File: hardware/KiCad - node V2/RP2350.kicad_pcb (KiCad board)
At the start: 4 copper layers, 55.6 x 52 mm, 83 parts, among them J1 Input, J2 Output, J3 USB_C_Receptacle_USB2.0_14P, J4 Screw_Terminal_01x08, SW1 BOOTSEL, U1 RP2350A, U2 THVD1450D, U3 ADXL355BEZ, U4 TPS2121RUXR, U5 USBLC6-2SC6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

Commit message: KiCad: J1 terminal update
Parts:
- added J5: IN/OUT Terminal, footprints:CONN-TH_B8B-XH-A-LF-SN, F.Cu at (176.5, 79.9)
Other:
- board size 55.6 x 52 mm -> 145.6 x 52.6 mm

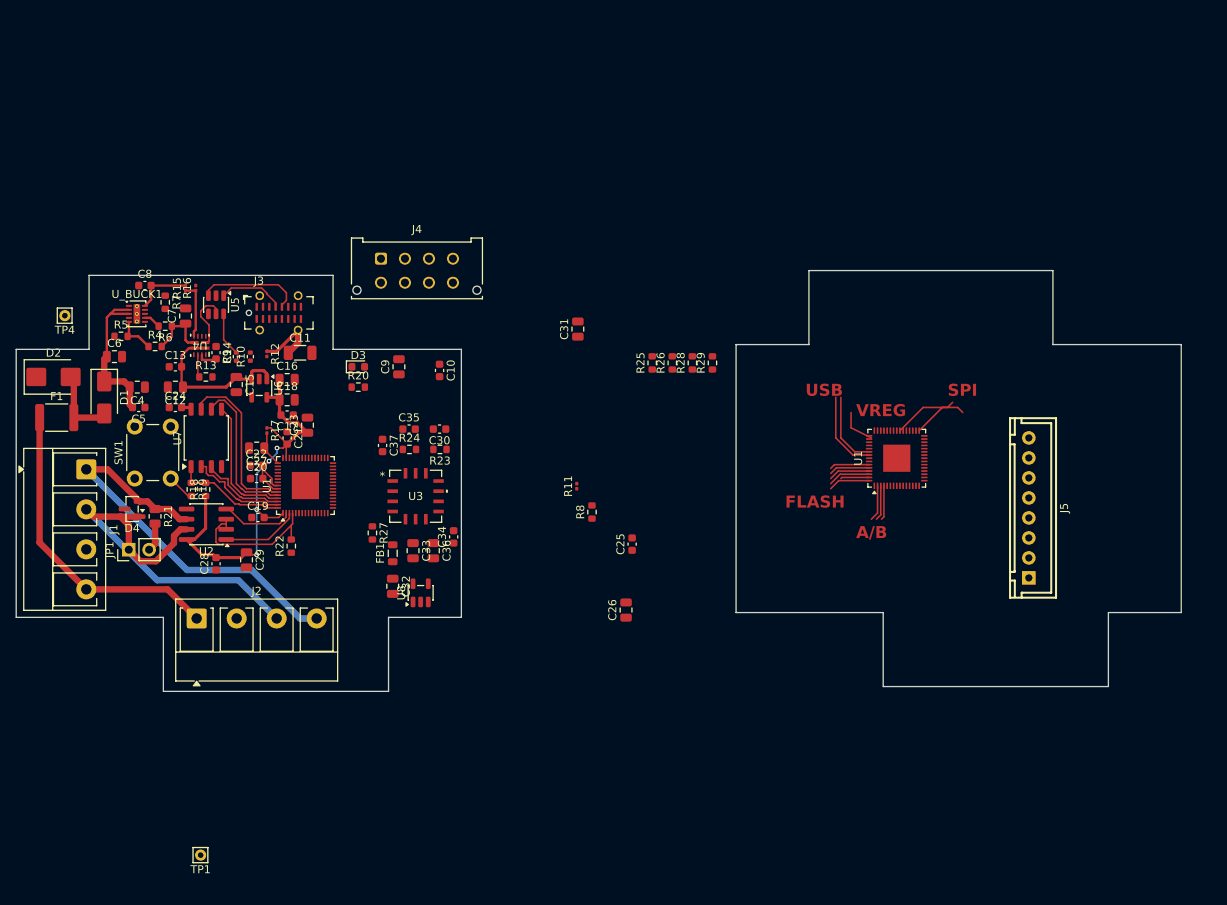
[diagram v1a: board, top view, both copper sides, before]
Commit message: hardware: added net classes
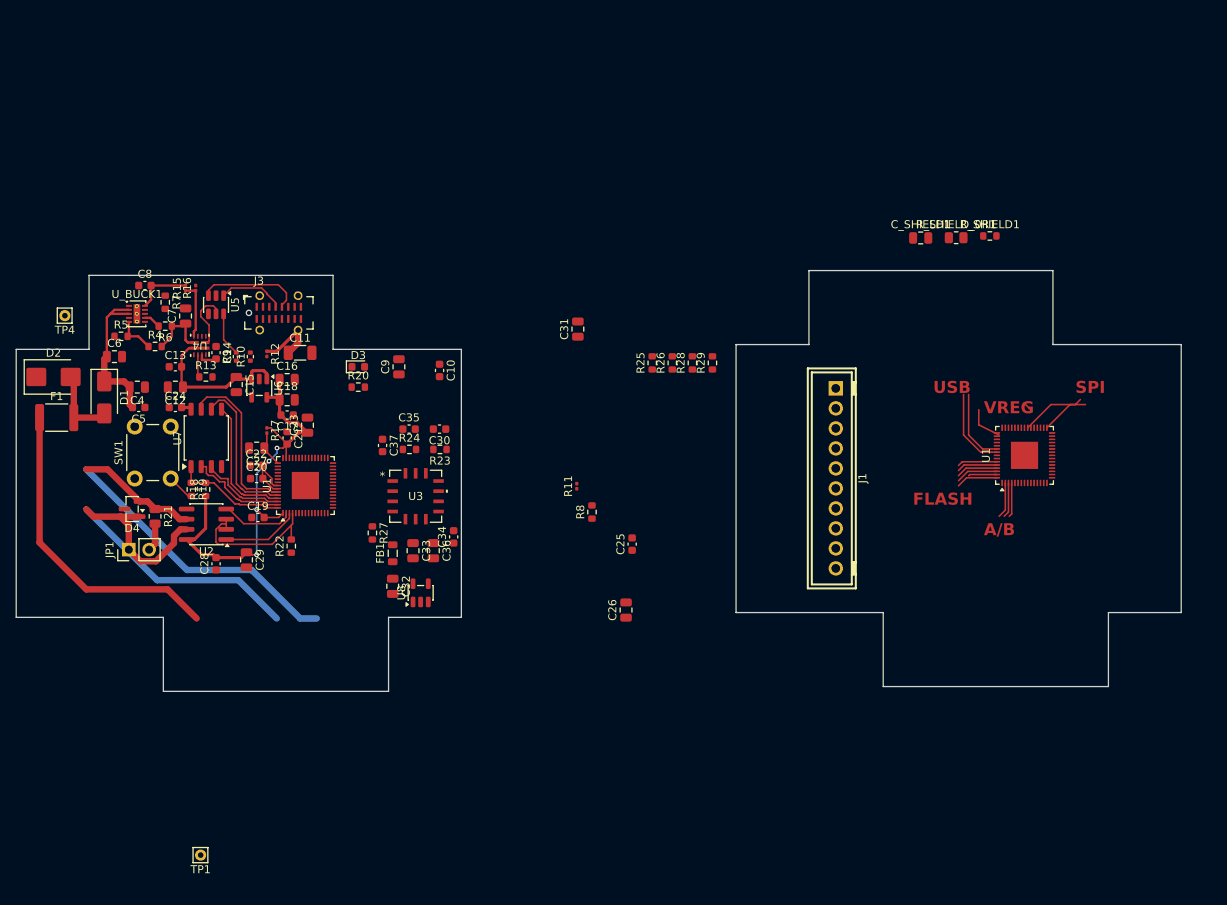
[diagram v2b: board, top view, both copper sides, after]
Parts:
- removed J2: Output, my_footprints:TerminalBlock_RND_205-00278_1x04_P5.00mm_Vertical
- removed J4: Screw_Terminal_01x08, Connector_Molex:Molex_Micro-Fit_3.0_43045-0812_2x04_P3.00mm_Vertical
- removed J5: IN/OUT Terminal, footprints:CONN-TH_B8B-XH-A-LF-SN
- added C_SHIELD1: 10nF, Capacitor_SMD:C_0805_2012Metric, F.Cu at (163.0, 46.1)
- added R_SHIELD1: 1M, Resistor_SMD:R_0603_1608Metric, F.Cu at (171.7, 45.9)
- added R_SHIELD_0R1: 0R DNP, Resistor_SMD:R_0805_2012Metric, F.Cu at (167.4, 46.1)
- J1: value Input -> JST-XH-10; footprint TerminalBlock_RND:TerminalBlock_RND_205-00278_1x04_P5.00mm_Vertical -> footprints:CONN-TH_10P-P2.50_B10B-XH-A-LF-SN
- moved J1 93.7 mm to (152.4, 76.2)
- moved U1 16.0 mm to (176.0, 73.3)
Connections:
- F1 pad 1: Net-(J1-12V) -> Net-(J1-12VIN)
- J1 pad 1: Net-(J1-12V) -> Net-(J1-12VIN)
- J1 pad 2: GND -> Net-(J1-12VIN)
- J1 pad 3: Net-(D4-A2) -> GND
- J1 pad 4: Net-(D4-A1) -> GND
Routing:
- net Net-(J1-12VIN): track 0.00 -> 39.2 mm
- net Net-(J1-12V): track 39.2 -> 0.00 mm

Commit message: hardware: 2 terminals fix
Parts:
- removed J1: JST-XH-10, footprints:CONN-TH_10P-P2.50_B10B-XH-A-LF-SN
- added J_IN1: JST-GH-5, footprints:CONN-SMD_BM05B-GHS-TBT, F.Cu at (189.2, 64.4)
- added J_OUT1: JST-GH-5, footprints:CONN-SMD_BM05B-GHS-TBT, F.Cu at (189.2, 70.7)
- moved F1 128.9 mm to (177.8, 29.4), turned to 90 degrees
- moved D4 125.2 mm to (189.6, 75.9), turned to -90 degrees
- moved D2 123.1 mm to (172.7, 28.6), turned to 90 degrees
- moved R_SHIELD_0R1 42.5 mm to (193.0, 80.0), turned to 180 degrees
- moved C_SHIELD1 41.6 mm to (193.0, 74.9), turned to 180 degrees
- moved R_SHIELD1 38.2 mm to (193.0, 77.5), turned to 180 degrees
- moved U1 15.9 mm to (167.7, 86.8), turned to 0 degrees
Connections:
- net Net-(D4-A1) renamed /RS485_B
- net Net-(D4-A2) renamed /RS485 A
- net Net-(J1-SH_IN) renamed /SHIELD
- F1 pad 1: Net-(J1-12VIN) -> /12V_BUS
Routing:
- net Net-(J1-12VIN): track 39.2 -> 0.00 mm
- net /RS485 A: track 51.6 -> 13.6 mm
- net (no net): track 15.0 -> 51.5 mm
- net /SHIELD: track 0.00 -> 14.2 mm
- net Net-(D1-A): track 9.27 -> 0.00 mm
- net GND: track 0.00 -> 6.35 mm, vias 0 -> 1
- net /12V_BUS: track 0.00 -> 6.35 mm
- net /RS485_B: track 51.1 -> 48.4 mm
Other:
- board size 145.6 x 52.6 mm -> 145.6 x 52 mm
- board text removed: "SPI"

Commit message: hardware: layout progress + many footprints
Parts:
- removed the U1 at (86.1, 77.1)
- added R2: 5.1k, Resistor_SMD:R_0402_1005Metric, F.Cu at (167.6, 68.7)
- added R3: 5.1k, Resistor_SMD:R_0402_1005Metric, F.Cu at (159.7, 62.4)
- C24: footprint Capacitor_SMD:C_0603_1608Metric -> Capacitor_SMD:C_0402_1005Metric
- J3: footprint my_footprints:USB_C_Receptacle_G-Switch_GT-USB-7051x -> footprints:USB-C-SMD_GT-USB-7051A
- R11: footprint Resistor_SMD:R_0201_0603Metric -> Resistor_SMD:R_0805_2012Metric
- R12: footprint Resistor_SMD:R_0201_0603Metric -> Resistor_SMD:R_0603_1608Metric
- SW1: footprint Button_Switch_THT:SW_PUSH_6mm -> footprints:KEY-SMD_4P-L4.2-W3.2-P2.20-LS4.6
- U5: footprint Package_TO_SOT_SMD:SOT-23-6 -> footprints:USBLC6-2SC6
- U7: footprint Package_SO:SOIC-8_5.3x5.3mm_P1.27mm -> footprints:WSON-8_L6.0-W5.0-P1.27-BL-EP
- moved D1 123.2 mm to (184.2, 64.8), turned to 90 degrees
- moved U6 111.2 mm to (190.8, 51.9)
- moved U2 103.5 mm to (177.2, 83.8), turned to 90 degrees
- moved U4 100.5 mm to (172.8, 70.6), turned to -90 degrees
- moved R12 94.4 mm to (175.7, 62.2), turned to 0 degrees
- moved SW1 92.0 mm to (155.9, 63.3), turned to 0 degrees
- moved U5 91.1 mm to (164.8, 69.7)
- moved U_BUCK1 90.9 mm to (155.9, 54.3)
- moved C11 87.3 mm to (172.7, 63.8), turned to -90 degrees
- moved R9 87.3 mm to (163.8, 73.7)
- moved R10 86.8 mm to (165.1, 73.7)
- moved J3 83.0 mm to (165.3, 64.0), turned to 180 degrees
- moved U7 82.8 mm to (156.5, 70.6), turned to 180 degrees
- moved R27 58.1 mm to (151.8, 73.0), turned to 90 degrees
- moved R11 57.2 mm to (175.9, 64.8), turned to 0 degrees
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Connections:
- C11 pad 1: Net-(J3-SHIELD) -> Net-(J3-SHELL)
- J3 pad A4: /USB_VBUS -> unconnected-(J3-VBUS-PadA4)
- J3 pad A8: (no net) -> unconnected-(J3-SBU1-PadA8)
- J3 pad A9: /USB_VBUS -> unconnected-(J3-VBUS-PadA9)
- J3 pad B4: /USB_VBUS -> unconnected-(J3-VBUS-PadB4)
- J3 pad B8: (no net) -> unconnected-(J3-SBU2-PadB8)
- R11 pad 1: Net-(J3-SHIELD) -> Net-(J3-SHELL)
- R12 pad 1: Net-(J3-SHIELD) -> Net-(J3-SHELL)
- U1 pad 2: Net-(U1-GPIO0) -> unconnected-(U1-GPIO0-Pad2)
- U1 pad 3: Net-(U1-GPIO1) -> unconnected-(U1-GPIO1-Pad3)
- U2 pad 1: Net-(U1-GPIO1) -> unconnected-(U2-RO-Pad1)
- U2 pad 4: Net-(U1-GPIO0) -> unconnected-(U2-DI-Pad4)
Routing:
- net /3V3_DIG: track 65.6 -> 0.00 mm, vias 4 -> 0
- net (no net): track 51.5 -> 0.00 mm
- net /RS485_B: track 48.4 -> 8.91 mm
- net Net-(U1-QSPI_SD3): track 25.8 -> 0.00 mm
- net Net-(U1-QSPI_SCLK): track 24.1 -> 0.00 mm
- net /5V_SYS: track 20.3 -> 0.00 mm
- net Net-(D1-K): track 19.8 -> 0.00 mm
- net GND: track 6.35 -> 25.6 mm, vias 1 -> 6
- net Net-(U1-QSPI_SD0): track 21.6 -> 5.19 mm
- net /5V_BUCK: track 15.4 -> 0.00 mm
- net Net-(U1-~{QSPI_SS}): track 19.6 -> 5.22 mm
- net Net-(U1-GPIO1): track 14.0 -> 0.00 mm
- net Net-(U1-GPIO2): track 22.6 -> 8.95 mm
- net Net-(U1-GPIO0): track 13.6 -> 0.00 mm
- net Net-(U1-QSPI_SD1): track 16.0 -> 3.59 mm
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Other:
- board text removed: "A/B"
- board text removed: "FLASH"
- board text removed: "USB"
- board text removed: "VREG"

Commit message: hardware: holly f
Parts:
- removed R8: 100k DNP, Resistor_SMD:R_0603_1608Metric
- added L2: 10uH, footprints:FXL0420-100-MIND-SMD_L4.4-W4.2, F.Cu at (174.3, 72.0)
- added L3: 3.3uH, footprints:IND-SMD_L2.0-W1.6_AOTA-B201610S3R3-101-T, F.Cu at (166.4, 77.2)
- R4, R5, R6, R7: footprint Resistor_SMD:R_0603_1608Metric -> Resistor_SMD:R_0402_1005Metric
- moved C6 120.2 mm to (182.2, 67.6), turned to -90 degrees
- moved C5 116.4 mm to (181.6, 63.0), turned to -90 degrees
- moved R5 116.3 mm to (179.1, 66.0), turned to -90 degrees
- moved JP1 114.5 mm to (177.1, 103.6)
- moved R21 114.5 mm to (180.3, 99.4)
- moved C4 114.0 mm to (179.1, 63.2), turned to -90 degrees
- moved R4 113.2 mm to (180.3, 66.0), turned to -90 degrees
- moved R6 108.8 mm to (176.9, 67.8), turned to -90 degrees
- moved R7 107.8 mm to (175.6, 67.8)
- moved C8 104.9 mm to (169.6, 69.2), turned to -90 degrees
- moved C7 102.1 mm to (172.5, 68.0), turned to 180 degrees
- moved R15 99.6 mm to (168.9, 71.5), turned to 0 degrees
- moved R16 98.6 mm to (168.9, 72.5), turned to 0 degrees
- moved R18 93.4 mm to (163.8, 53.3)
- moved R19 93.4 mm to (162.0, 53.3)
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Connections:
- R7 pad 1: GND -> /5V_BUCK
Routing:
- net GND: track 25.6 -> 63.9 mm, vias 6 -> 10
- net /5V_BUCK: track 0.00 -> 30.6 mm
- net Net-(U1-QSPI_SD3): track 0.00 -> 14.8 mm
- net Net-(D1-K): track 0.00 -> 12.8 mm
- net Net-(U1-QSPI_SCLK): track 0.00 -> 12.6 mm
- net /SHIELD: track 6.35 -> 16.6 mm
- net Net-(D1-A): track 0.00 -> 9.26 mm
- net Net-(U1-GPIO2): track 8.95 -> 0.00 mm
- net Net-(U_BUCK1-SW): track 0.00 -> 7.04 mm
- net /12V_BUS: track 6.35 -> 11.8 mm
- net Net-(U_BUCK1-FB): track 0.00 -> 4.75 mm
- net unconnected-(U1-GPIO0-Pad2): track 4.49 -> 0.00 mm
- net unconnected-(U1-GPIO1-Pad3): track 4.39 -> 0.00 mm
- net Net-(U1-QSPI_SD0): track 5.19 -> 9.10 mm
- net Net-(J3-DP1): track 4.87 -> 8.48 mm
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
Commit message: hardware: train update
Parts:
- removed C10, C8: 100nF, Capacitor_SMD:C_0603_1608Metric
- removed C12, C9: 22uF, Capacitor_SMD:C_0805_2012Metric
- removed R13: 80k, my_footprints:R_0603_1608Metric
- removed R15: 100k, Resistor_SMD:R_0201_0603Metric
- removed R16: 47k, Resistor_SMD:R_0201_0603Metric
- removed R18: 10k DNP, my_footprints:R_0603_1608Metric
- removed R19: 1k, my_footprints:R_0603_1608Metric
- added C_IN1: 100nF, Capacitor_SMD:C_0402_1005Metric, F.Cu at (168.9, 68.4)
- added C_IN2: 100nF, Capacitor_SMD:C_0402_1005Metric, F.Cu at (166.8, 74.6)
- added C_OUT1: 22uF, Capacitor_SMD:C_0805_2012Metric, F.Cu at (165.1, 75.1)
- added C_USB_BULK1: 22uF, Capacitor_SMD:C_0805_2012Metric, F.Cu at (169.2, 74.7)
- added R14: 10k, Resistor_SMD:R_0402_1005Metric, F.Cu at (164.7, 69.4)
- added R_ILM1: 100k, Resistor_SMD:R_0402_1005Metric, F.Cu at (164.4, 70.9)
- added R_PR1_BOT1: 100k, Resistor_SMD:R_0402_1005Metric, F.Cu at (170.5, 70.3)
- added R_PR1_TOP1: 324k, Resistor_SMD:R_0402_1005Metric, F.Cu at (170.5, 72.3)
- C13: footprint Capacitor_SMD:C_0603_1608Metric -> Capacitor_SMD:C_0402_1005Metric
- moved C28 99.6 mm to (174.3, 81.5), turned to -90 degrees
- moved C29 97.9 mm to (176.5, 81.3), turned to 90 degrees
- moved C15 96.2 mm to (171.4, 85.1)
- moved C13 96.1 mm to (165.8, 67.9)
- moved C14 89.7 mm to (163.8, 72.4), turned to 0 degrees
- moved C17 51.8 mm to (134.6, 78.4)
- moved C18 51.8 mm to (134.6, 76.5)
- moved C19 51.8 mm to (131.0, 91.2)
- moved C21 51.8 mm to (134.6, 81.3)
- moved C22 51.8 mm to (130.8, 84.7)
- moved R17 51.8 mm to (132.1, 80.4)
- moved C20 51.8 mm to (130.8, 86.4)
- moved C23 51.8 mm to (137.2, 79.7)
- moved C27 51.8 mm to (130.8, 82.5)
- moved C16 50.4 mm to (133.0, 74.9)
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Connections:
- net Net-(J3-DN1) renamed /USB DN
- net Net-(J3-DP1) renamed /USB DP
- D4 pad 2: /RS485 A -> /RS485_A
- J_IN1 pad 3: /RS485 A -> /RS485_B
- J_IN1 pad 4: /RS485_B -> /RS485_A
- J_OUT1 pad 2: GND -> unconnected-(J_OUT1-GND-Pad2)
- J_OUT1 pad 3: /RS485 A -> /RS485_B
- J_OUT1 pad 4: /RS485_B -> /RS485_A
- J_OUT1 pad 5: /SHIELD -> unconnected-(J_OUT1-SHIELD-Pad5)
- R21 pad 1: /RS485 A -> /RS485_A
- SW1 pad 2: Net-(R19-Pad2) -> Net-(U1-~{QSPI_SS})
- U2 pad 6: /RS485 A -> /RS485_A
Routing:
- net GND: track 63.9 -> 87.3 mm, vias 10 -> 16
- net /RS485_B: track 6.35 -> 29.4 mm
- net /RS485_A: track 0.00 -> 22.8 mm
- net /USB_VBUS: track 2.25 -> 24.0 mm, vias 1 -> 3
- net Net-(U1-~{QSPI_SS}): track 4.96 -> 15.0 mm
- net /3V3_DIG: track 0.00 -> 8.35 mm, vias 0 -> 1
- net /5V_BUCK: track 30.6 -> 37.2 mm
- net /RS485 A: track 6.35 -> 0.00 mm
- net /5V_SYS: track 1.35 -> 7.20 mm, vias 0 -> 1
- net Net-(JP1-B): track 0.00 -> 4.52 mm
- net Net-(U4-SS): track 0.00 -> 1.79 mm
- net Net-(U4-ST): track 0.00 -> 1.65 mm
- net Net-(U4-ILM): track 0.00 -> 1.34 mm
- net Net-(U1-GPIO2): track 0.00 -> 1.27 mm
- net Net-(J3-CC1): track 3.61 -> 4.63 mm
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
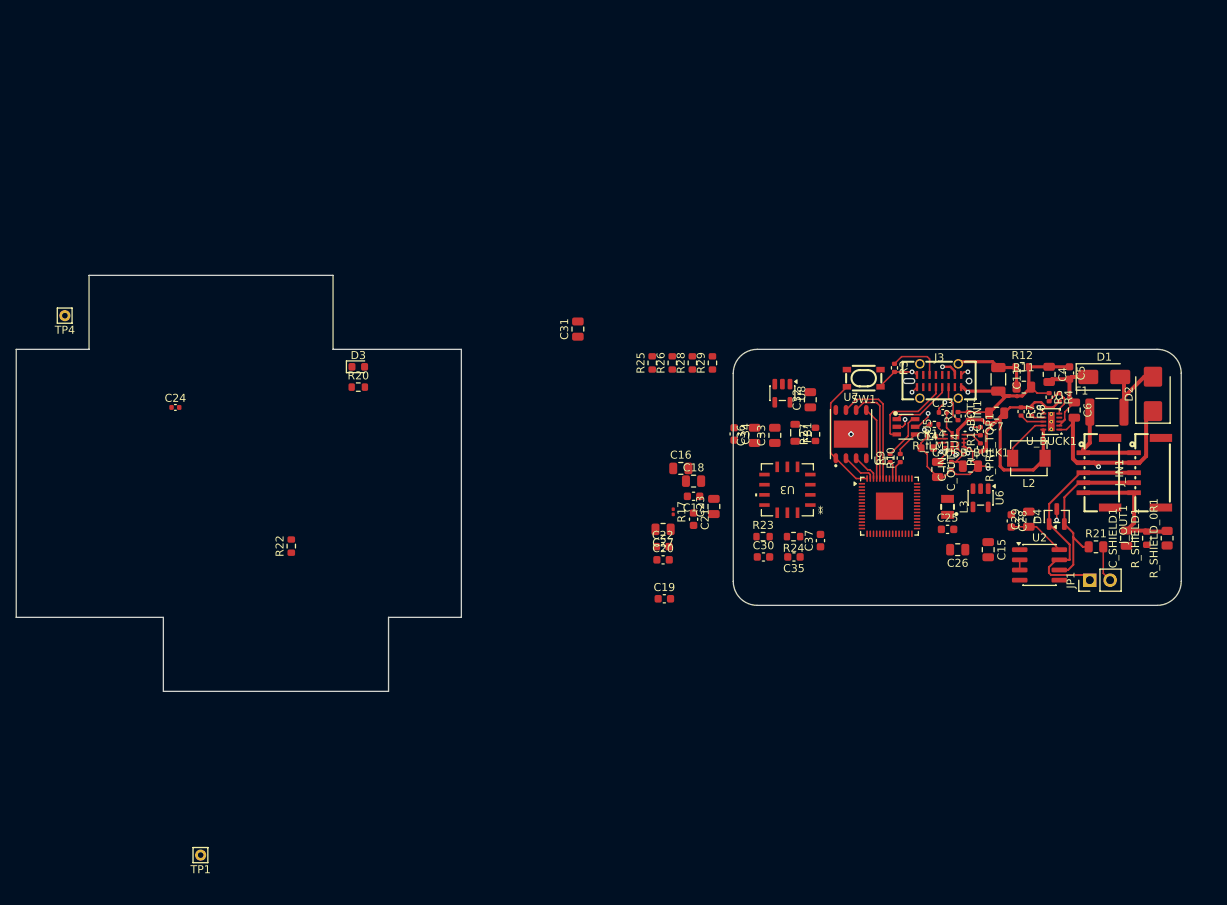
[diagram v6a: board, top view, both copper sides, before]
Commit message: hardware: 3v3_dig, 1vcore
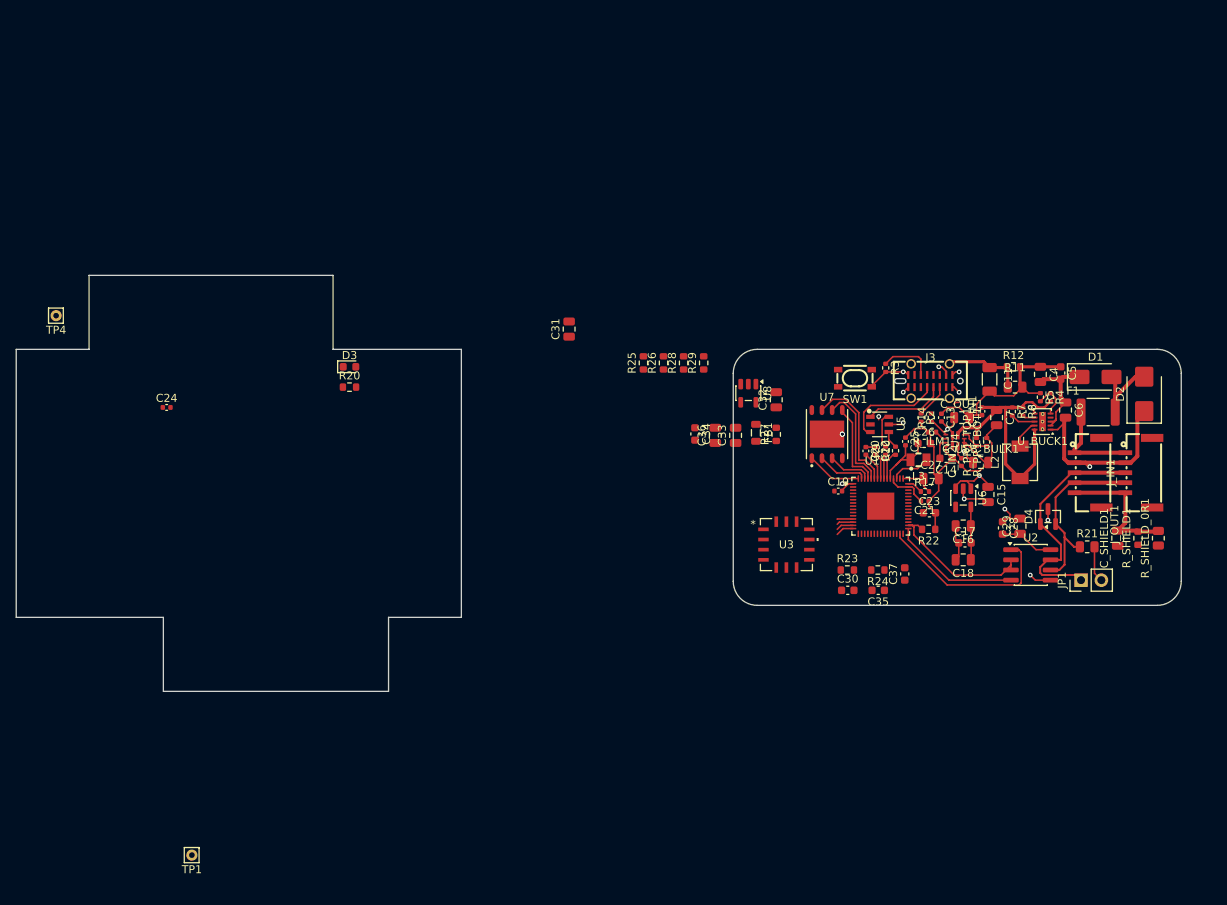
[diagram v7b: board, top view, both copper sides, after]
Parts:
- C19, C20, C21, C22, C25: footprint Capacitor_SMD:C_0603_1608Metric -> Capacitor_SMD:C_0402_1005Metric
- C23, C26: footprint Capacitor_SMD:C_0805_2012Metric -> Capacitor_SMD:C_0603_1608Metric
- R17: footprint Resistor_SMD:R_0201_0603Metric -> Resistor_SMD:R_0402_1005Metric
- moved R22 79.7 mm to (164.0, 82.5), turned to 180 degrees
- moved C16 36.0 mm to (168.3, 82.1), turned to 180 degrees
- moved C18 35.1 mm to (168.3, 86.4), turned to 180 degrees
- moved C17 34.4 mm to (168.5, 84.2), turned to 0 degrees
- moved C27 34.1 mm to (164.3, 76.2), turned to 0 degrees
- moved R17 31.6 mm to (163.5, 77.8), turned to 0 degrees
- moved C22 29.2 mm to (157.4, 72.7), turned to -90 degrees
- moved C21 29.0 mm to (163.5, 79.0), turned to 180 degrees
- moved C20 28.8 mm to (156.2, 72.7), turned to -90 degrees
- moved C23 27.0 mm to (164.1, 80.5), turned to 0 degrees
- moved C19 25.6 mm to (152.7, 77.8)
- moved C26 13.9 mm to (163.5, 71.8), turned to 0 degrees
- moved C25 12.2 mm to (161.1, 71.6), turned to -90 degrees
- moved C30 11.3 mm to (153.9, 90.2)
- moved C35 11.3 mm to (157.7, 90.2)
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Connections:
- J3 pad A4: unconnected-(J3-VBUS-PadA4) -> /USB_VBUS
- J3 pad A9: unconnected-(J3-VBUS-PadA9) -> /USB_VBUS
- J3 pad B4: unconnected-(J3-VBUS-PadB4) -> /USB_VBUS
- R22 pad 2: Net-(U1-GPIO2) -> Net-(U1-GPIO20)
- R26 pad 2: Net-(U1-GPIO9) -> Net-(U1-GPIO20)
- U1 pad 13: Net-(U1-GPIO9) -> Net-(U1-GPIO20)
- U1 pad 29: unconnected-(U1-GPIO18-Pad29) -> Net-(U1-GPIO18)
- U1 pad 31: unconnected-(U1-GPIO19-Pad31) -> Net-(U1-GPIO19)
- U1 pad 32: unconnected-(U1-GPIO20-Pad32) -> Net-(U1-GPIO20)
- U1 pad 4: Net-(U1-GPIO2) -> unconnected-(U1-GPIO2-Pad4)
- U2 pad 1: unconnected-(U2-RO-Pad1) -> Net-(U1-GPIO18)
- U2 pad 2: Net-(U1-GPIO2) -> Net-(U1-GPIO20)
- U2 pad 3: Net-(U1-GPIO2) -> Net-(U1-GPIO20)
- U2 pad 4: unconnected-(U2-DI-Pad4) -> Net-(U1-GPIO19)
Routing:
- net GND: track 87.3 -> 118.0 mm, vias 16 -> 14
- net Net-(U1-GPIO18): track 0.00 -> 23.5 mm
- net /3V3_DIG: track 8.35 -> 30.2 mm
- net Net-(U1-GPIO20): track 0.00 -> 21.8 mm
- net Net-(U1-GPIO19): track 0.00 -> 16.3 mm
- net /5V_SYS: track 7.20 -> 21.8 mm, vias 1 -> 2
- net /1V1_CORE: track 0.00 -> 9.47 mm
- net Net-(U1-~{QSPI_SS}): track 15.0 -> 6.87 mm
- net Net-(U1-VREG_LX): track 0.00 -> 4.98 mm
- net Net-(U1-VREG_AVDD): track 0.00 -> 4.46 mm
- net /USB_VBUS: track 24.0 -> 27.6 mm
- net /5V_BUCK: track 37.2 -> 34.3 mm
- net Net-(U_BUCK1-SW): track 6.27 -> 3.54 mm
- net /USB DP: track 7.74 -> 10.1 mm
- net Net-(U1-GPIO11): track 0.00 -> 2.29 mm
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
